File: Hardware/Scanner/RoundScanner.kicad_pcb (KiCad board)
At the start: 4 copper layers, 45 x 42.5 mm, 79 parts, among them J1 I2C ThroughHole, J3 I2C, J4 Interface, Q1 BSS138DW-7-F, U1 OPA2376xxD, U2 NAU7802SGI, U4 OPA2376xxD, U5 TLC59208FIPWR, U6 AS7341-DLGT, U7 AP7312-1833W6-7, U9 AP2127N-2.5, X1 4.9152 MHz

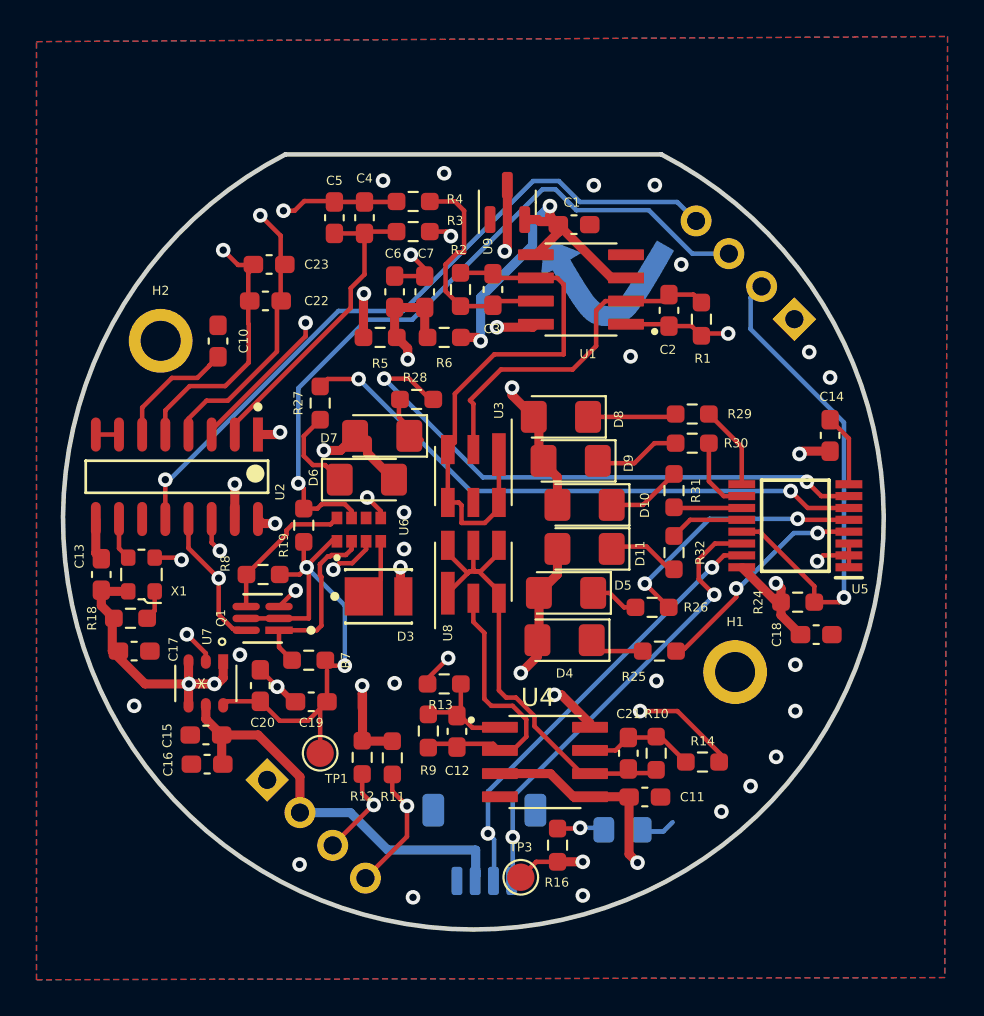
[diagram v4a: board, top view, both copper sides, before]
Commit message: updated schematic, and layout, updated bom, fully converted to 3.3v for Voltage input only
Signed-off-by: lokimetasmith <lokimail@gmail.com>
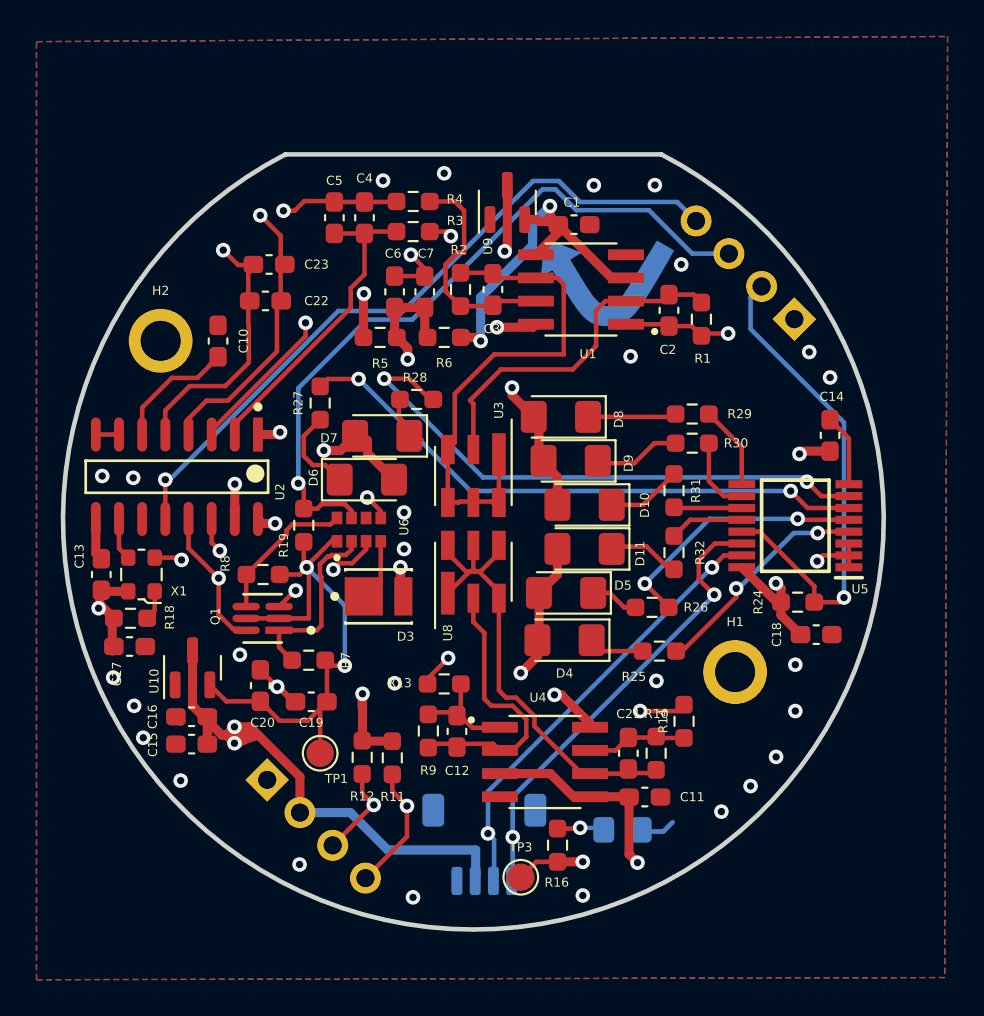
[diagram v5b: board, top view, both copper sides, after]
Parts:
- removed U7: AP7312-1833W6-7, AP7312-1833W6-7:AP7312-1833W6-7
- added U10: AP2127N-1.8, Package_TO_SOT_SMD:SOT-23, F.Cu at (73.9, 115.5)
- C1, C11, C16, C18: value 100nF -> 0.1uF
- R25: value 56 -> 43
- R26, R29, R30: value 150 -> 43
- R27, R28: value 240 -> 43
- R31: value 40 -> 43
- R32: value 130 -> 43
- U3: value ~ -> MTSM2601SMF1-100
- U8: value ~ -> MTSM1346SMF1-100
- moved C16 2.74 mm to (73.8, 118.2)
- moved R14 2.45 mm to (100.8, 118.4), turned to 90 degrees
- moved C15 0.93 mm to (73.8, 119.7)
- moved C17 0.35 mm to (70.4, 114.3)
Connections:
- C15 pad 2: VCC -> +3.3V
- C16 pad 2: VCC -> +3.3V
- J1 pad 2: VCC -> +3.3V
- J3 pad 2: VCC -> +3.3V
- U3 pad 5: unconnected-(U3-NC-Pad5) -> /InGaS Sensor/Cathode
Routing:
- net VCC: track 22.7 -> 0.00 mm
- net +3.3V: track 65.4 -> 87.0 mm, vias 15 -> 16
- net /ADC/AIN2+: track 60.1 -> 57.0 mm
- net GND: track 26.9 -> 25.3 mm, vias 29 -> 33
- net /InGaS Sensor/Cathode: track 28.7 -> 27.5 mm
- net +1V8: track 30.0 -> 31.0 mm
- net Net-(C21-Pad2): track 5.84 -> 5.19 mm

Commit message: added decoupling capactitors, added footprint for 3d model, need to verify new footprint
Signed-off-by: lokimetasmith <lokimail@gmail.com>
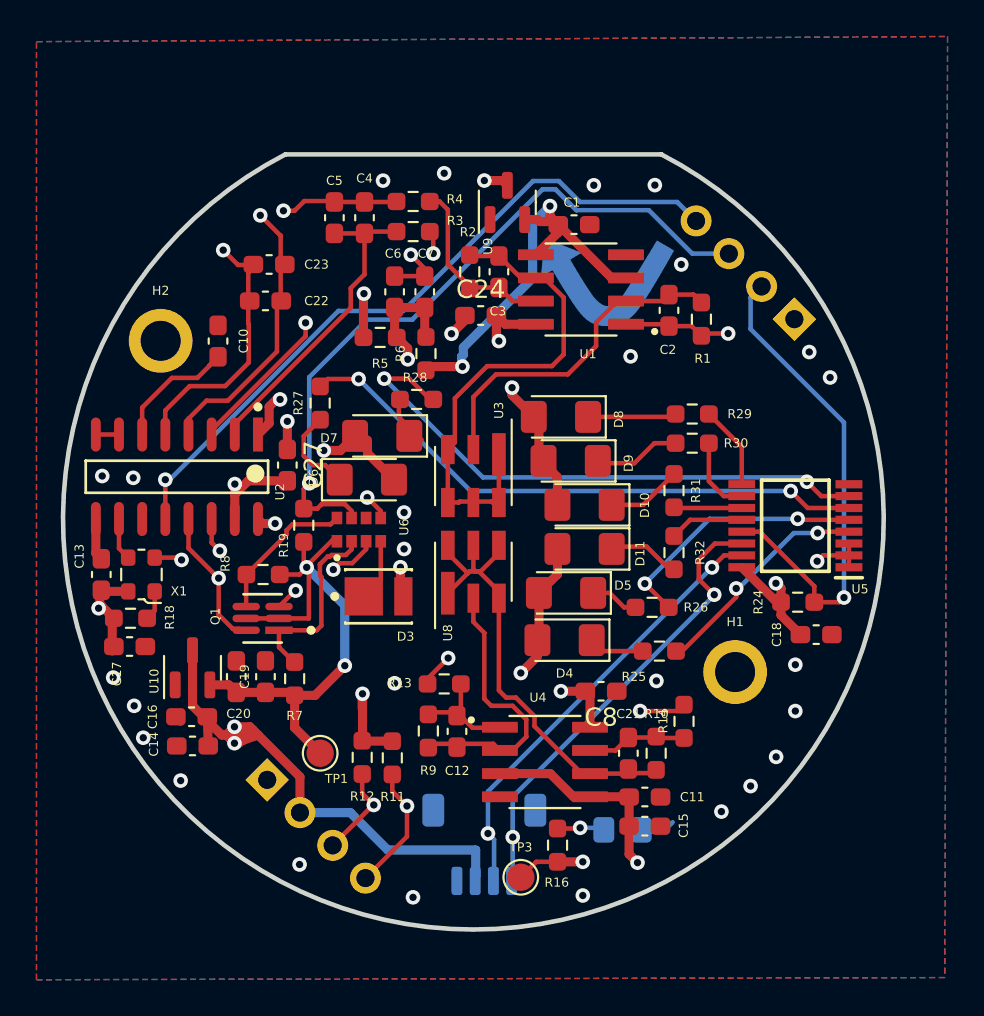
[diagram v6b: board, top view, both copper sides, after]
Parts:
- added C24: 1uF, Capacitor_SMD:C_0603_1608Metric_Pad1.08x0.95mm_HandSolder, F.Cu at (89.7, 96.2)
- added C27: 0.1uF, Capacitor_SMD:C_0603_1608Metric_Pad1.08x0.95mm_HandSolder, F.Cu at (79.1, 104.4)
- added C8: 1uF, Capacitor_SMD:C_0603_1608Metric_Pad1.08x0.95mm_HandSolder, F.Cu at (96.3, 116.8)
- J3: value I2C -> SM04B-SRSS-TB
- R16: value 150 -> 1k
- moved C14 38.9 mm to (73.9, 119.8), turned to 0 degrees
- moved C15 25.3 mm to (98.7, 124.2), turned to 180 degrees
- moved C19 2.86 mm to (77.9, 116.0), turned to -90 degrees
- moved C20 1.40 mm to (76.3, 116.0)
- moved R6 1.34 mm to (86.7, 98.3), turned to -90 degrees
- moved R7 1.27 mm to (79.5, 116.1), turned to 90 degrees
- moved R2 1.10 mm to (89.1, 93.8)
- moved C3 1.03 mm to (90.7, 93.8)
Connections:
- C15 pad 2: +3.3V -> VDDA
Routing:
- net GND: track 25.3 -> 20.4 mm
- net Net-(U2-AVDD/LDO): track 22.0 -> 24.3 mm
- net Net-(C3-Pad2): track 12.1 -> 9.95 mm
- net +3.3V: track 87.0 -> 88.7 mm, vias 16 -> 15
- net VDDA: track 66.0 -> 67.4 mm
- net +1V8: track 31.0 -> 29.9 mm
- net /InGaS Sensor/Anode: track 18.7 -> 18.2 mm

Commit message: cleared all DRC errors
Signed-off-by: lokimetasmith <lokimail@gmail.com>
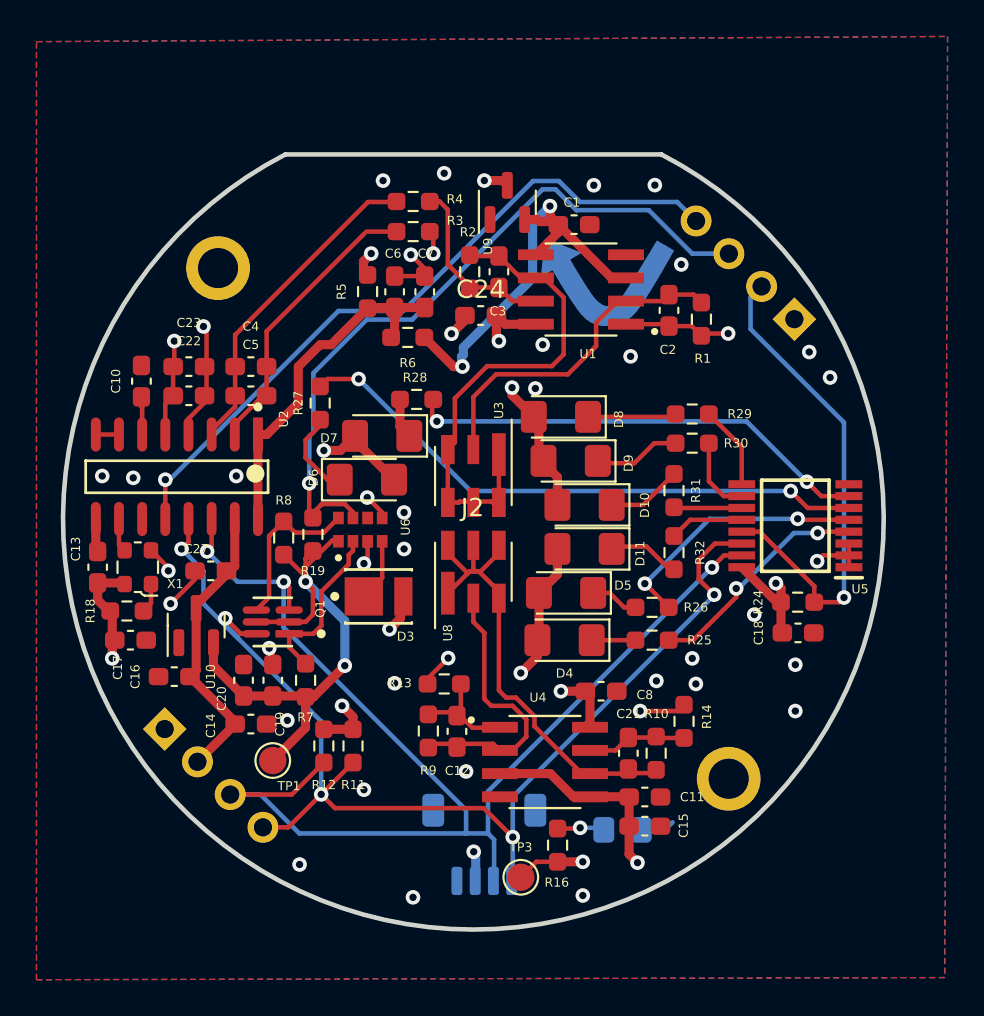
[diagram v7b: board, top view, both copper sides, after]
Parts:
- removed H1, H2: MountingHole, MountingHole:MountingHole_2.2mm_M2_ISO7380_Pad
- removed J1: I2C ThroughHole, Connector_PinSocket_2.54mm:PinSocket_1x04_P2.54mm_Vertical
- removed J4: Interface, Connector_PinSocket_2.54mm:PinSocket_1x04_P2.54mm_Vertical
- added J2: Conn_01x09, round_module:round_notch, F.Cu at (89.3, 107.6)
- moved C5 10.8 mm to (77.1, 100.6), turned to 180 degrees
- moved C4 10.3 mm to (77.1, 99.0), turned to 0 degrees
- moved C27 7.16 mm to (74.9, 110.2), turned to 0 degrees
- moved C23 7.12 mm to (73.7, 99.0)
- moved C22 6.68 mm to (73.7, 100.6)
- moved C10 4.74 mm to (71.1, 99.8)
- moved C14 3.42 mm to (77.1, 118.6), turned to 180 degrees
- moved TP1 2.63 mm to (78.3, 120.6)
- moved R5 2.60 mm to (83.5, 94.9), turned to 90 degrees
- moved C16 2.40 mm to (72.9, 116.0)
- moved U10 2.32 mm to (74.1, 113.2)
- moved R8 2.30 mm to (78.9, 108.4), turned to 90 degrees
- moved R11 2.25 mm to (82.7, 119.8)
- moved R12 2.20 mm to (81.1, 119.8)
- moved R6 1.34 mm to (85.7, 97.4), turned to 0 degrees
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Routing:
- net +3.3V: track 88.7 -> 68.5 mm, vias 15 -> 13
- net /ADC/AIN2-: track 45.4 -> 34.3 mm
- net /ADC/AIN2+: track 57.0 -> 47.0 mm
- net SDA: track 62.6 -> 71.4 mm, vias 5 -> 3
- net Net-(U5-~{OUT3}): track 31.3 -> 25.5 mm
- net Net-(U2-VBG): track 6.80 -> 2.08 mm
- net /ADC/AIN+: track 21.0 -> 17.6 mm, vias 2 -> 0
- net Net-(U2-AVDD/LDO): track 24.3 -> 21.2 mm, vias 3 -> 0
- net SCL: track 62.6 -> 64.8 mm, vias 4 -> 5
- net +1V8: track 29.9 -> 31.7 mm
- net /ADC/AIN-: track 16.7 -> 15.0 mm
- net /MCU + IO/SCL_2v: track 10.3 -> 9.30 mm
- net /MCU + IO/SDA_2v: track 8.12 -> 9.07 mm
- net VDDA: track 67.4 -> 68.1 mm
- net Net-(D4-K): track 3.05 -> 2.40 mm
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
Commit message: as ordered 11/27/2023 from JLCPCB
Updated silk on RoundScanner, minor changes,

major changes on control board, cleaned up foot prints, nudged parts around
control board not ready for release yet
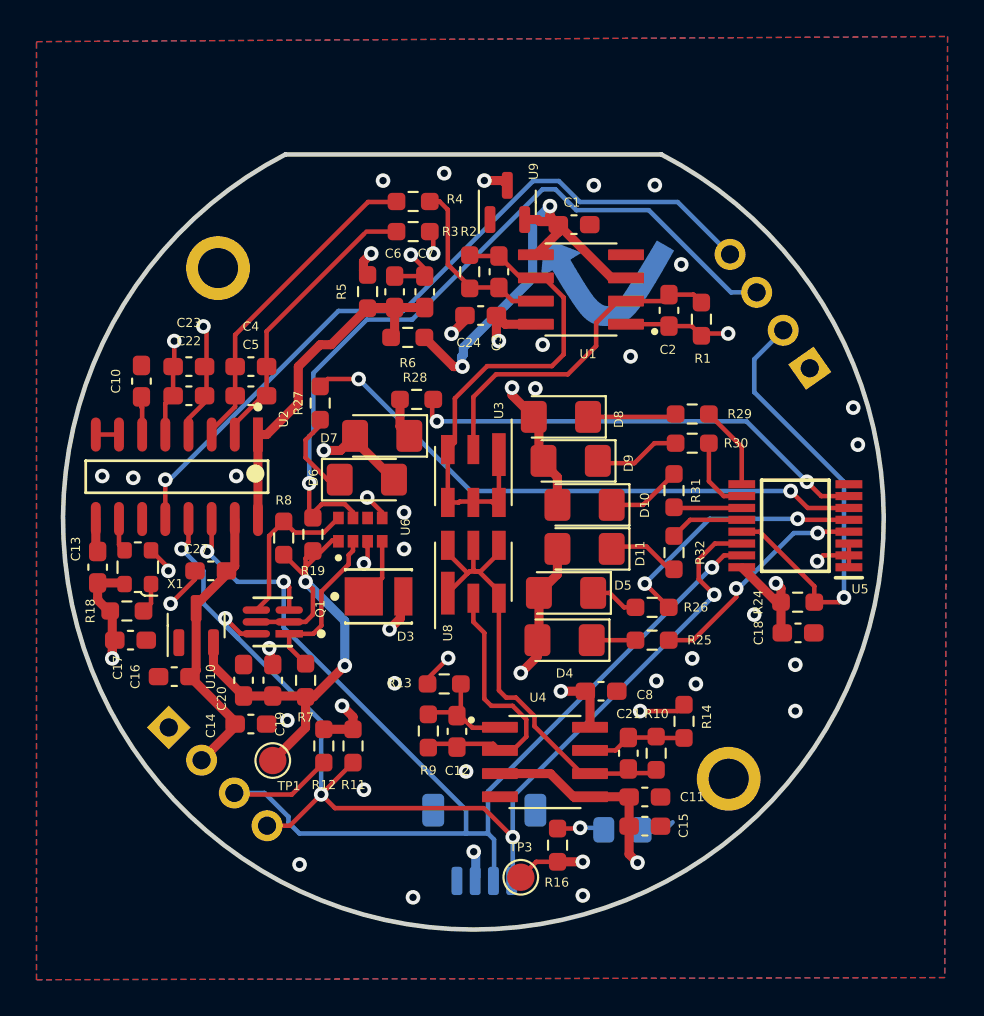
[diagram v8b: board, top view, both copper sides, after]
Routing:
- net /ADC/DRDY_INT: track 38.9 -> 41.6 mm
- net /MCU + IO/AS7341_INT: track 39.7 -> 42.1 mm
- net /LED/LED_RESET: track 27.3 -> 25.2 mm
